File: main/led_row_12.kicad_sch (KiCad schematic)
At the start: 30 parts

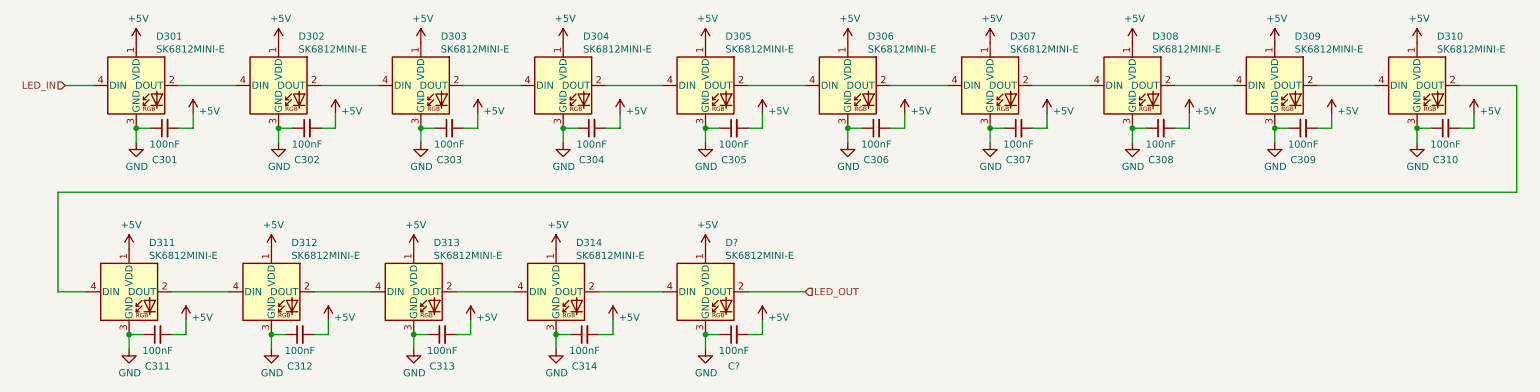
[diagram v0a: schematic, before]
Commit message: Start placing components
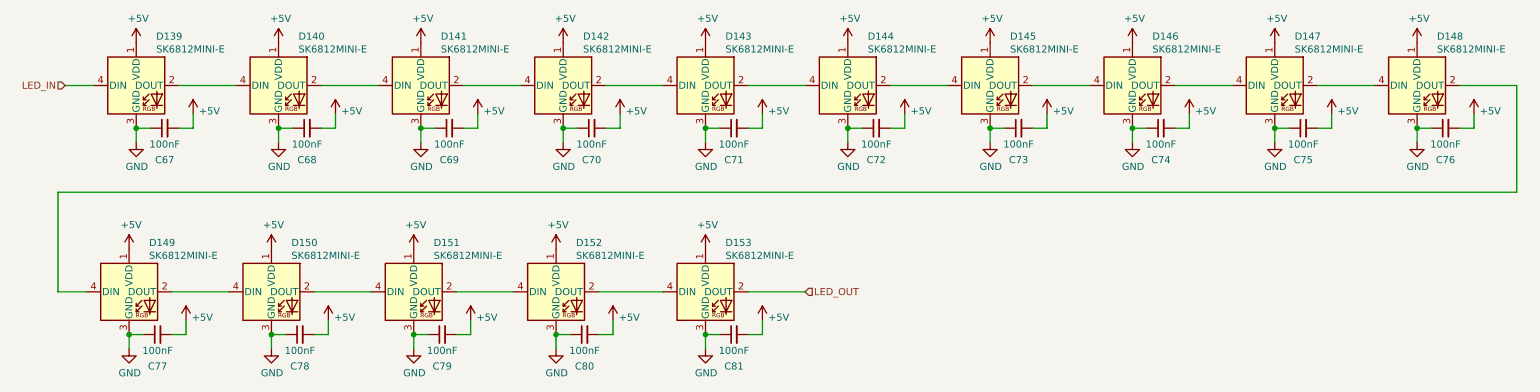
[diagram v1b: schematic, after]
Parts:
- C67: renamed from C301; footprint (none) -> Capacitor_SMD:C_0603_1608Metric
- C68: renamed from C302; footprint (none) -> Capacitor_SMD:C_0603_1608Metric
- C69: renamed from C303; footprint (none) -> Capacitor_SMD:C_0603_1608Metric
- C70: renamed from C304; footprint (none) -> Capacitor_SMD:C_0603_1608Metric
- C71: renamed from C305; footprint (none) -> Capacitor_SMD:C_0603_1608Metric
- C72: renamed from C306; footprint (none) -> Capacitor_SMD:C_0603_1608Metric
- C73: renamed from C307; footprint (none) -> Capacitor_SMD:C_0603_1608Metric
- C74: renamed from C308; footprint (none) -> Capacitor_SMD:C_0603_1608Metric
- C75: renamed from C309; footprint (none) -> Capacitor_SMD:C_0603_1608Metric
- C76: renamed from C310; footprint (none) -> Capacitor_SMD:C_0603_1608Metric
- C77: renamed from C311; footprint (none) -> Capacitor_SMD:C_0603_1608Metric
- C78: renamed from C312; footprint (none) -> Capacitor_SMD:C_0603_1608Metric
- C79: renamed from C313; footprint (none) -> Capacitor_SMD:C_0603_1608Metric
- C80: renamed from C314; footprint (none) -> Capacitor_SMD:C_0603_1608Metric
- C81: renamed from C?; footprint (none) -> Capacitor_SMD:C_0603_1608Metric
- D139: renamed from D301; footprint bigbutton:LED_SK6812_MINI_E_REVERSE -> chonc60:LED_SK6812_MINI_E_REVERSE
- D140: renamed from D302; footprint bigbutton:LED_SK6812_MINI_E_REVERSE -> chonc60:LED_SK6812_MINI_E_REVERSE
- D141: renamed from D303; footprint bigbutton:LED_SK6812_MINI_E_REVERSE -> chonc60:LED_SK6812_MINI_E_REVERSE
- D142: renamed from D304; footprint bigbutton:LED_SK6812_MINI_E_REVERSE -> chonc60:LED_SK6812_MINI_E_REVERSE
- D143: renamed from D305; footprint bigbutton:LED_SK6812_MINI_E_REVERSE -> chonc60:LED_SK6812_MINI_E_REVERSE
- D144: renamed from D306; footprint bigbutton:LED_SK6812_MINI_E_REVERSE -> chonc60:LED_SK6812_MINI_E_REVERSE
- D145: renamed from D307; footprint bigbutton:LED_SK6812_MINI_E_REVERSE -> chonc60:LED_SK6812_MINI_E_REVERSE
- D146: renamed from D308; footprint bigbutton:LED_SK6812_MINI_E_REVERSE -> chonc60:LED_SK6812_MINI_E_REVERSE
- D147: renamed from D309; footprint bigbutton:LED_SK6812_MINI_E_REVERSE -> chonc60:LED_SK6812_MINI_E_REVERSE
- D148: renamed from D310; footprint bigbutton:LED_SK6812_MINI_E_REVERSE -> chonc60:LED_SK6812_MINI_E_REVERSE
- D149: renamed from D311; footprint bigbutton:LED_SK6812_MINI_E_REVERSE -> chonc60:LED_SK6812_MINI_E_REVERSE
- D150: renamed from D312; footprint bigbutton:LED_SK6812_MINI_E_REVERSE -> chonc60:LED_SK6812_MINI_E_REVERSE
- D151: renamed from D313; footprint bigbutton:LED_SK6812_MINI_E_REVERSE -> chonc60:LED_SK6812_MINI_E_REVERSE
- D152: renamed from D314; footprint bigbutton:LED_SK6812_MINI_E_REVERSE -> chonc60:LED_SK6812_MINI_E_REVERSE
- D153: renamed from D?; footprint bigbutton:LED_SK6812_MINI_E_REVERSE -> chonc60:LED_SK6812_MINI_E_REVERSE

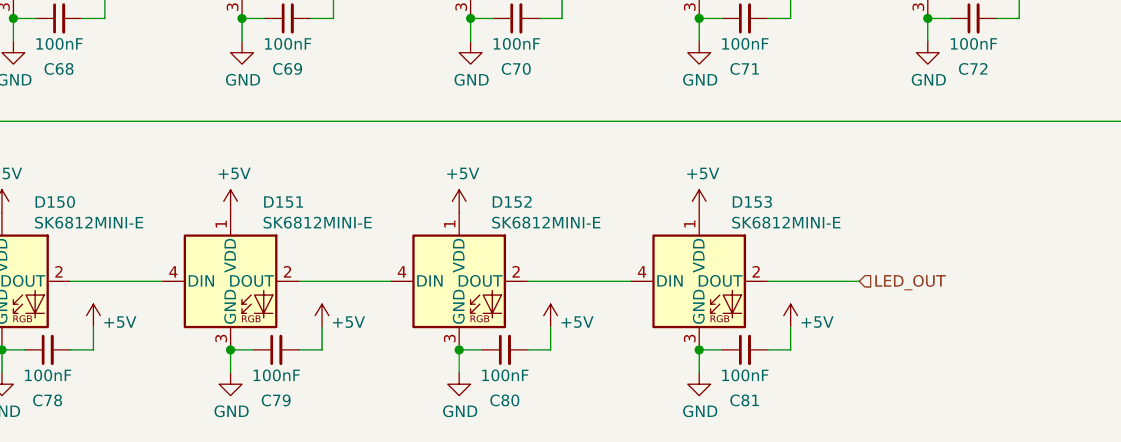
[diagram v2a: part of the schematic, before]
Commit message: Place diodes
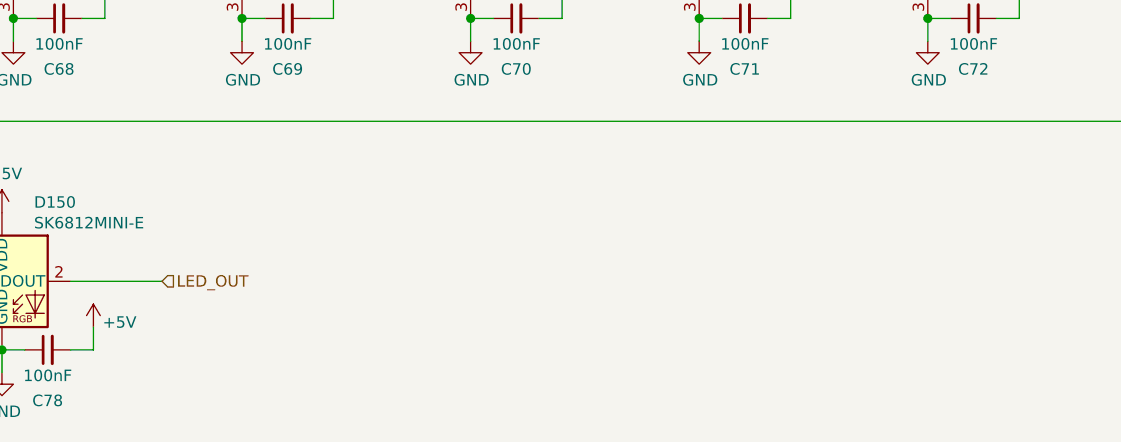
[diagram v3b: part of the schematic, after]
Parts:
- removed C79, C80, C81: 100nF, Capacitor_SMD:C_0603_1608Metric, symbol Device:C_Small
- removed D151, D152, D153: SK6812MINI-E, chonc60:LED_SK6812_MINI_E_REVERSE, symbol chonc60:SK6812MINI-E
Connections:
- net LED_OUT: now also D150.2 (DOUT)

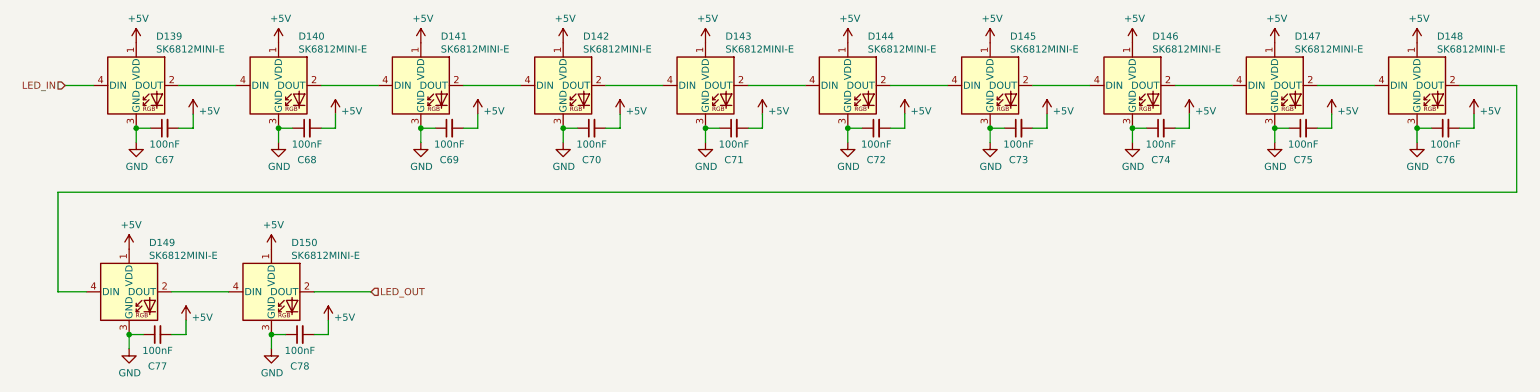
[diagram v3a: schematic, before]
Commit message: Place LEDs, start routing
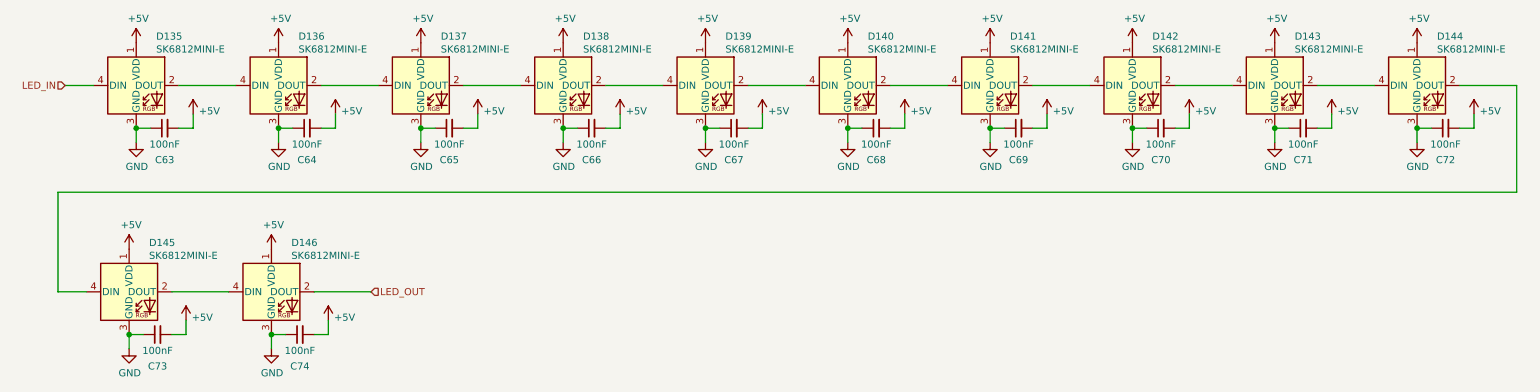
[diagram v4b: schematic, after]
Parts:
- renumbered C67 to C63, C68 to C64, C69 to C65, C70 to C66, C71 to C67, C72 to C68, C73 to C69, C74 to C70, C75 to C71, C76 to C72, C77 to C73, C78 to C74, D139 to D135, D140 to D136, D141 to D137, D142 to D138, D143 to D139, D144 to D140, D145 to D141, D146 to D142, D147 to D143, D148 to D144, D149 to D145, D150 to D146
